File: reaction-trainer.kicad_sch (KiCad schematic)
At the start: 2 parts

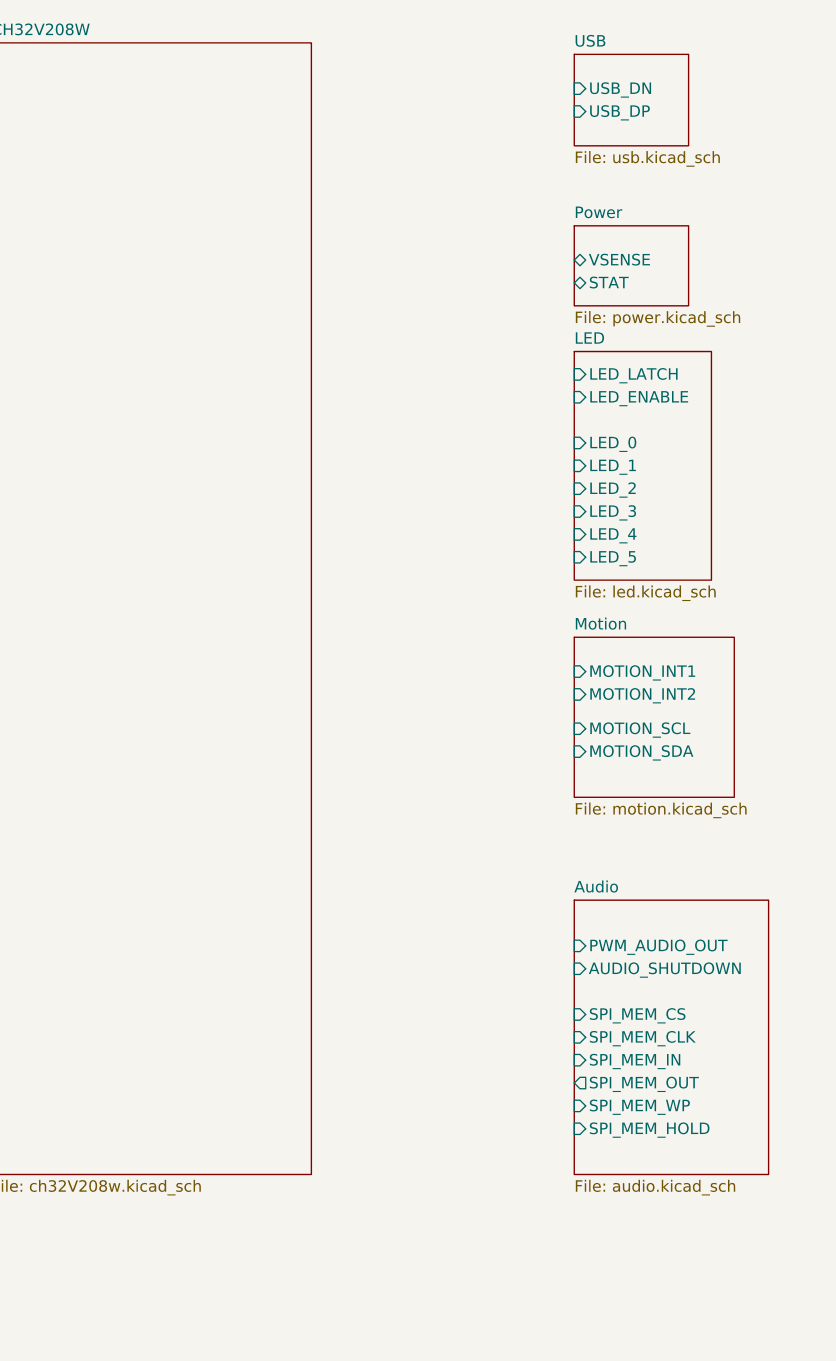
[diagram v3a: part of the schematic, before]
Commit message: Removed audio, more routing
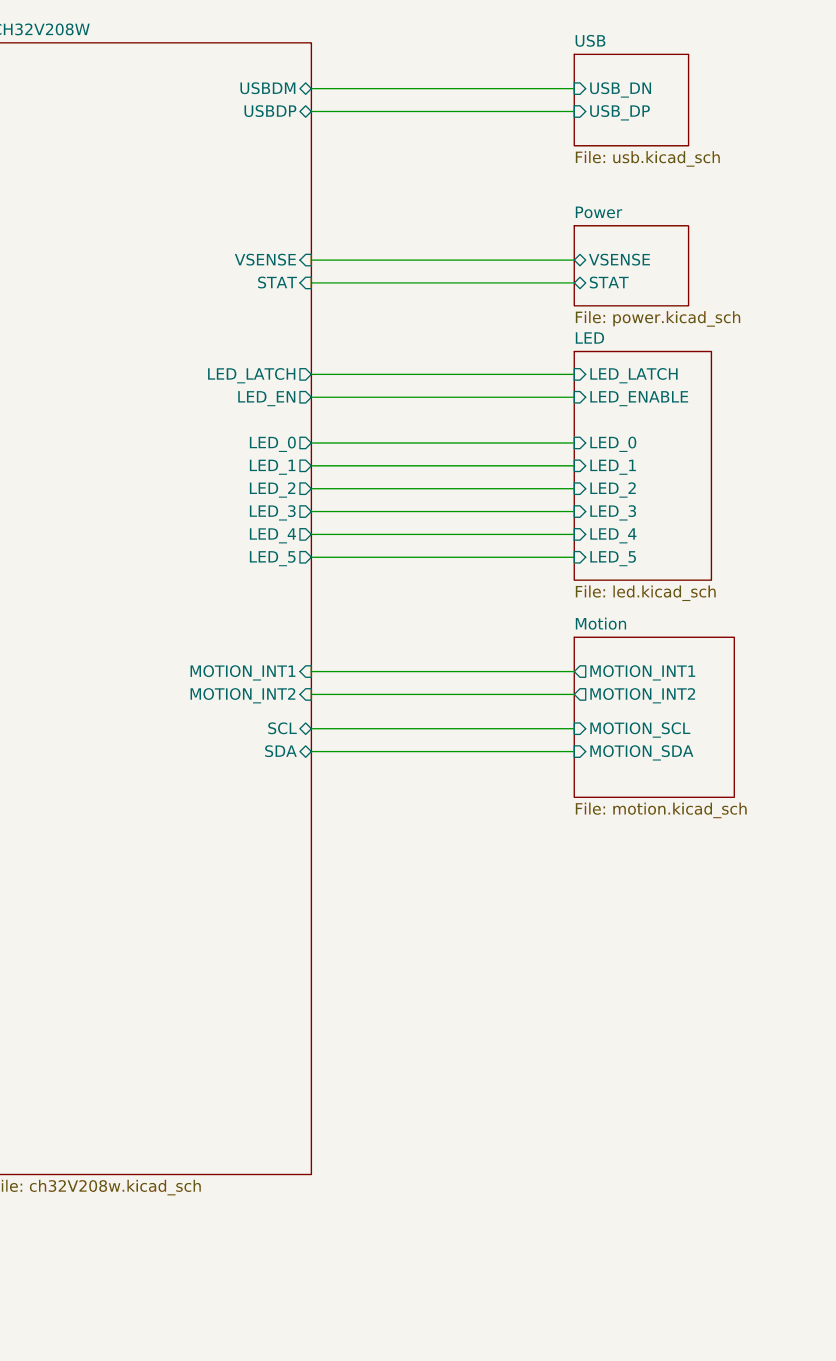
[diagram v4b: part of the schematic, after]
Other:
- removed sheet Audio
- sheet CH32V208W ports: added LED_0, LED_1, LED_2, LED_3, LED_4, LED_5, LED_EN, LED_LATCH, MOTION_INT1, MOTION_INT2, SCL, SDA, STAT, USBDM, USBDP, VSENSE; removed none
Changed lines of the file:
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@@
   (junction (at 41.91 179.07) (diameter 0) (color 0 0 0 0)
   )
+  (wire (pts (xy 125.73 72.39) (xy 154.94 72.39))
+    (stroke (width 0) (type default))
+  )
+  (wire (pts (xy 125.73 82.55) (xy 154.94 82.55))
+    (stroke (width 0) (type default))
+  )
+  (wire (pts (xy 125.73 62.23) (xy 154.94 62.23))
+    (stroke (width 0) (type default))
+  )
   (wire (pts (xy 36.83 179.07) (xy 41.91 179.07))
     (stroke (width 0) (type default))
   )
+  (wire (pts (xy 125.73 52.07) (xy 154.94 52.07))
+    (stroke (width 0) (type default))
+  )
+  (wire (pts (xy 125.73 101.6) (xy 154.94 101.6))
+    (stroke (width 0) (type default))
+  )
+  (wire (pts (xy 125.73 74.93) (xy 154.94 74.93))
+    (stroke (width 0) (type default))
+  )
+  (wire (pts (xy 125.73 97.79) (xy 154.94 97.79))
+    (stroke (width 0) (type default))
+  )
+  (wire (pts (xy 125.73 95.25) (xy 154.94 95.25))
+    (stroke (width 0) (type default))
+  )
+  (wire (pts (xy 125.73 80.01) (xy 154.94 80.01))
+    (stroke (width 0) (type default))
+  )
+  (wire (pts (xy 125.73 30.48) (xy 154.94 30.48))
+    (stroke (width 0) (type default))
+  )
+  (wire (pts (xy 125.73 77.47) (xy 154.94 77.47))
+    (stroke (width 0) (type default))
+  )
+  (wire (pts (xy 125.73 64.77) (xy 154.94 64.77))
+    (stroke (width 0) (type default))
+  )
+  (wire (pts (xy 125.73 104.14) (xy 154.94 104.14))
+    (stroke (width 0) (type default))
+  )
   (wire (pts (xy 41.91 179.07) (xy 45.72 179.07))
+    (stroke (width 0) (type default))
+  )
+  (wire (pts (xy 125.73 49.53) (xy 154.94 49.53))
+    (stroke (width 0) (type default))
+  )
+  (wire (pts (xy 125.73 69.85) (xy 154.94 69.85))
+    (stroke (width 0) (type default))
+  )
+  (wire (pts (xy 125.73 33.02) (xy 154.94 33.02))
     (stroke (width 0) (type default))
   )
@@
       (effects (font (size 1.27 1.27)) (justify left top))
     )
-    (pin "MOTION_INT1" input (at 154.94 95.25 180)
-      (effects (font (size 1.27 1.27)) (justify left))
-    )
-    (pin "MOTION_INT2" input (at 154.94 97.79 180)
+    (pin "MOTION_INT1" output (at 154.94 95.25 180)
+      (effects (font (size 1.27 1.27)) (justify left))
+    )
+    (pin "MOTION_INT2" output (at 154.94 97.79 180)
       (effects (font (size 1.27 1.27)) (justify left))
     )
@@
     )
   )
-  (sheet (at 154.94 120.65) (size 21.59 30.48) (fields_autoplaced)
-    (stroke (width 0.1524) (type solid))
-    (fill (color 0 0 0 0.0000))
-    (property "Sheetname" "Audio" (at 154.94 119.9384 0)
-      (effects (font (size 1.27 1.27)) (justify left bottom))
-    )
-    (property "Sheetfile" "audio.kicad_sch" (at 154.94 151.7146 0)
-      (effects (font (size 1.27 1.27)) (justify left top))
-    )
-    (pin "PWM_AUDIO_OUT" input (at 154.94 125.73 180)
-      (effects (font (size 1.27 1.27)) (justify left))
-    )
-    (pin "SPI_MEM_CS" input (at 154.94 133.35 180)
-      (effects (font (size 1.27 1.27)) (justify left))
-    )
-    (pin "SPI_MEM_CLK" input (at 154.94 135.89 180)
-      (effects (font (size 1.27 1.27)) (justify left))
-    )
-    (pin "SPI_MEM_IN" input (at 154.94 138.43 180)
-      (effects (font (size 1.27 1.27)) (justify left))
-    )
-    (pin "SPI_MEM_OUT" output (at 154.94 140.97 180)
-      (effects (font (size 1.27 1.27)) (justify left))
-    )
-    (pin "SPI_MEM_WP" input (at 154.94 143.51 180)
-      (effects (font (size 1.27 1.27)) (justify left))
-    )
-    (pin "SPI_MEM_HOLD" input (at 154.94 146.05 180)
-      (effects (font (size 1.27 1.27)) (justify left))
-    )
-    (pin "AUDIO_SHUTDOWN" input (at 154.94 128.27 180)
-      (effects (font (size 1.27 1.27)) (justify left))
-    )
-    (instances
-      (project "reaction-trainer"
-        (path "/726cb70d-0185-4970-973b-037545fc3942" (page "7"))
-      )
-    )
-  )
   (sheet (at 90.17 25.4) (size 35.56 125.73) (fields_autoplaced)
     (stroke (width 0.1524) (type solid))
@@
       (effects (font (size 1.27 1.27)) (justify left top))
     )
-    (instances
+    (pin "LED_5" output (at 125.73 82.55 0)
+      (effects (font (size 1.27 1.27)) (justify right))
+    )
+    (pin "LED_4" output (at 125.73 80.01 0)
+      (effects (font (size 1.27 1.27)) (justify right))
+    )
+    (pin "LED_LATCH" output (at 125.73 62.23 0)
+      (effects (font (size 1.27 1.27)) (justify right))
+    )
+    (pin "LED_3" output (at 125.73 77.47 0)
+      (effects (font (size 1.27 1.27)) (justify right))
+    )
+    (pin "LED_2" output (at 125.73 74.93 0)
+      (effects (font (size 1.27 1.27)) (justify right))
+    )
+    (pin "LED_1" output (at 125.73 72.39 0)
+      (effects (font (size 1.27 1.27)) (justify right))
+    )
+    (pin "LED_0" output (at 125.73 69.85 0)
+      (effects (font (size 1.27 1.27)) (justify right))
+    )
+    (pin "LED_EN" output (at 125.73 64.77 0)
+      (effects (font (size 1.27 1.27)) (justify right))
+    )
+    (pin "USBDM" bidirectional (at 125.73 30.48 0)
+      (effects (font (size 1.27 1.27)) (justify right))
+    )
+    (pin "USBDP" bidirectional (at 125.73 33.02 0)
+      (effects (font (size 1.27 1.27)) (justify right))
+    )
+    (pin "STAT" input (at 125.73 52.07 0)
+      (effects (font (size 1.27 1.27)) (justify right))
+    )
+    (pin "VSENSE" input (at 125.73 49.53 0)
+      (effects (font (size 1.27 1.27)) (justify right))
+    )
+    (pin "MOTION_INT1" input (at 125.73 95.25 0)
+      (effects (font (size 1.27 1.27)) (justify right))
+    )
+    (pin "MOTION_INT2" input (at 125.73 97.79 0)
+      (effects (font (size 1.27 1.27)) (justify right))
+    )
+    (pin "SCL" bidirectional (at 125.73 101.6 0)
+      (effects (font (size 1.27 1.27)) (justify right))
+    )
+    (pin "SDA" bidirectional (at 125.73 104.14 0)
+      (effects (font (size 1.27 1.27)) (justify right))
+    )
+    (instances
